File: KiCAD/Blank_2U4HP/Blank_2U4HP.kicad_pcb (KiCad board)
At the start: 2 copper layers, 20 x 84 mm, 2 parts

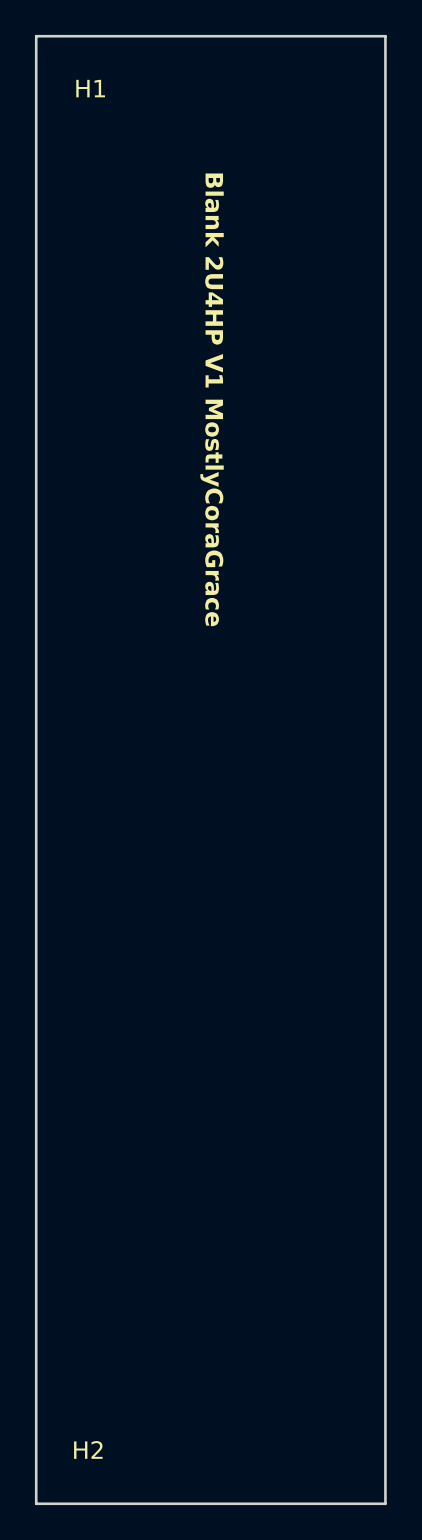
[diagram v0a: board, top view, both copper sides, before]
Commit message: removed all front silkscreen, and flipped most modules, to make the boards 'cleaner'.
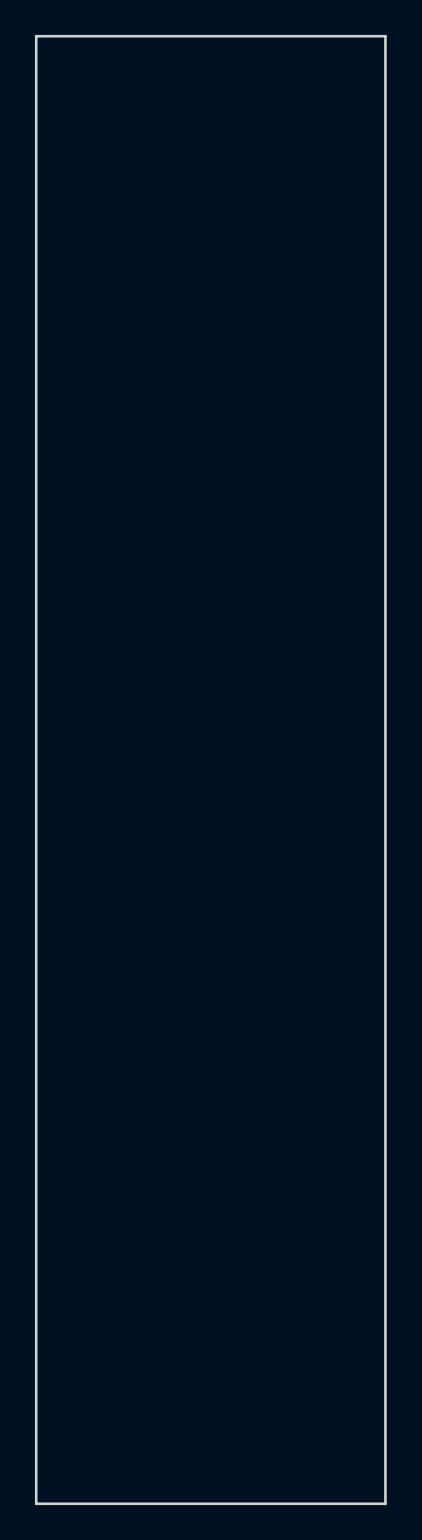
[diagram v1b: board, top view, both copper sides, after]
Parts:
- H1, H2: moved to B.Cu
- turned H1 to 180 degrees
- turned H2 to 180 degrees

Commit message: added copper fills to every module, to maybe possibly increase structural rigidity.
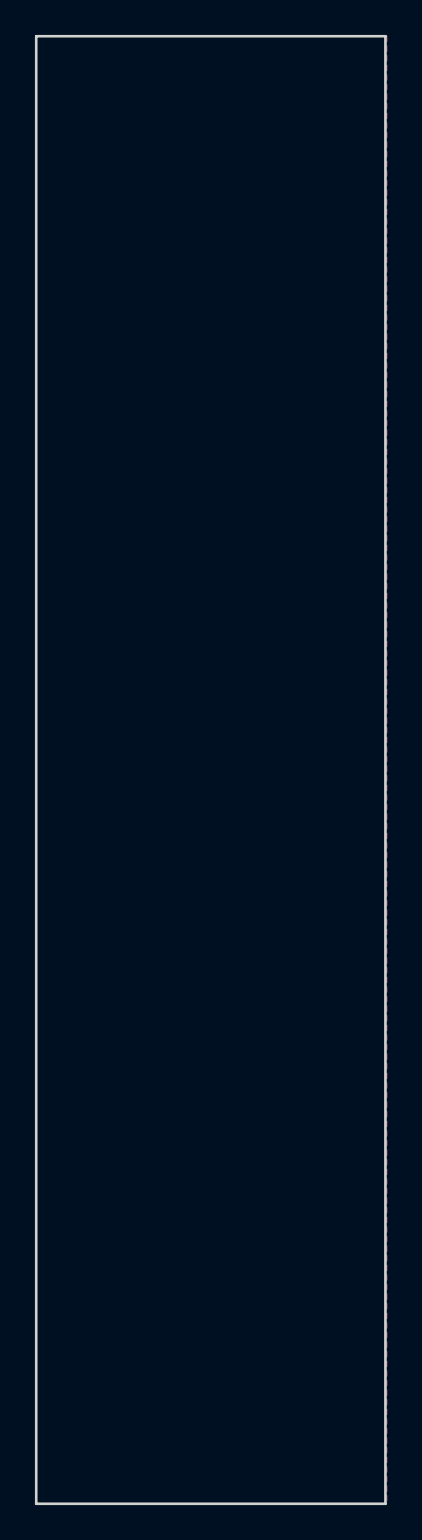
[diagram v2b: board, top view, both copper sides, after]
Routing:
- added copper zone on B.Cu, net (none)
- added copper zone on F.Cu, net (none)
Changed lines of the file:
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@@
+		)
+	)
+	(zone
+		(net 0)
+		(net_name "")
+		(layers "F&B.Cu")
+		(hatch edge 0.5)
+		(connect_pads
+			(clearance 0.5)
+		)
+		(min_thickness 0.25)
+		(filled_areas_thickness no)
+		(fill yes
+			(thermal_gap 0.5)
+			(thermal_bridge_width 0.5)
+			(island_removal_mode 1)
+			(island_area_min 10)
+		)
+		(polygon
+			(pts
+				(xy 0 2.413) (xy 20.066 2.413) (xy 20.066 86.487) (xy 0 86.487)
+			)
 		)
 	)
